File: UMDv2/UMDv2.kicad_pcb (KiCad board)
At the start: 2 copper layers, 128.3 x 83.8 mm, 115 parts, among them CON201 USB-B1HSB6, CON302 JTAG-2X10-HDR, CON303 101-00405-75, CON304 UMDv2-CONN, CON305 HDR1X2, CON306 HDR1X3, SW301 PTS645SM43SMTR92_LFS, U201 MIC5504-3.3YM5-TR, U202 TPS2115APWR, U203 TPS25921ADR, U205 AZ1117CH-3.3TRG1, U207 INA199A2DCKR, U301 STM32F413ZHT6, U302 74ALVC164245DL,118, U303 74ALVC164245DL,118, X301 ECS-80-18-30-JGN-TR

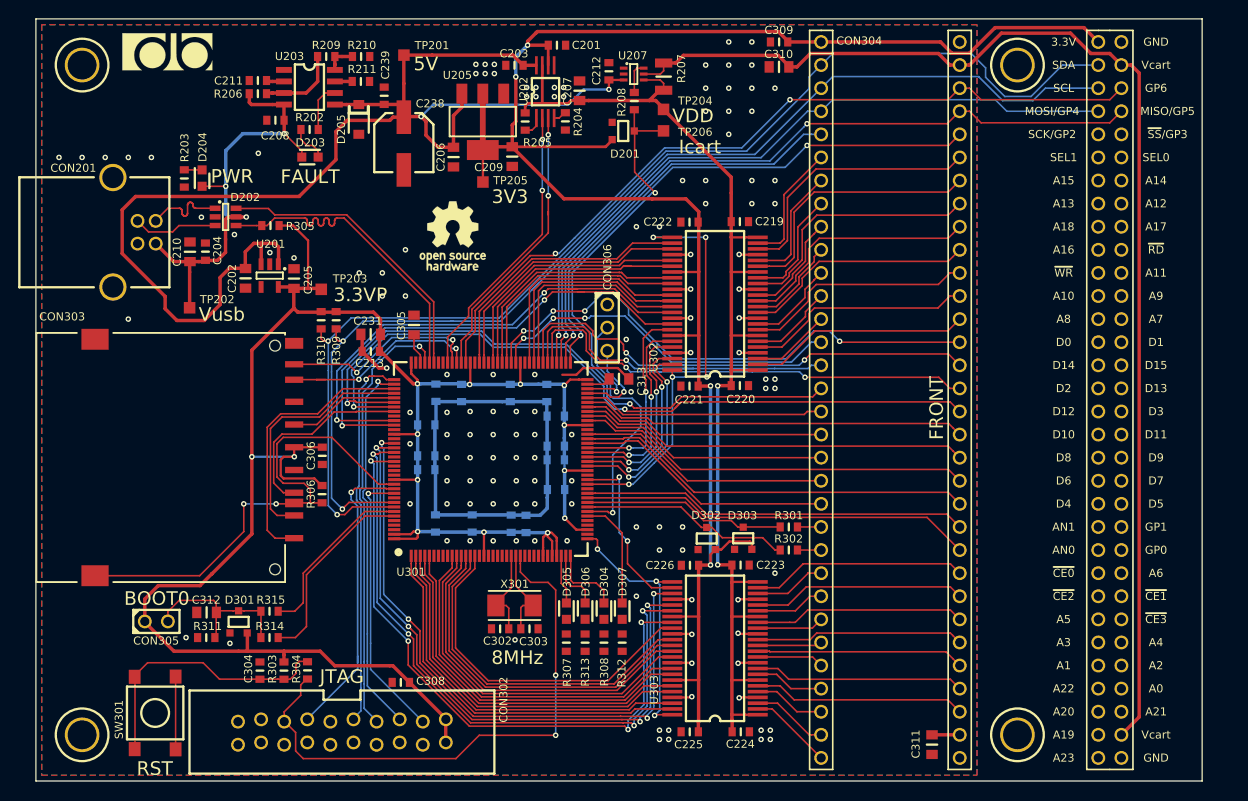
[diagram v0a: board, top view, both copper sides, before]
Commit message: finished LA connector, started review
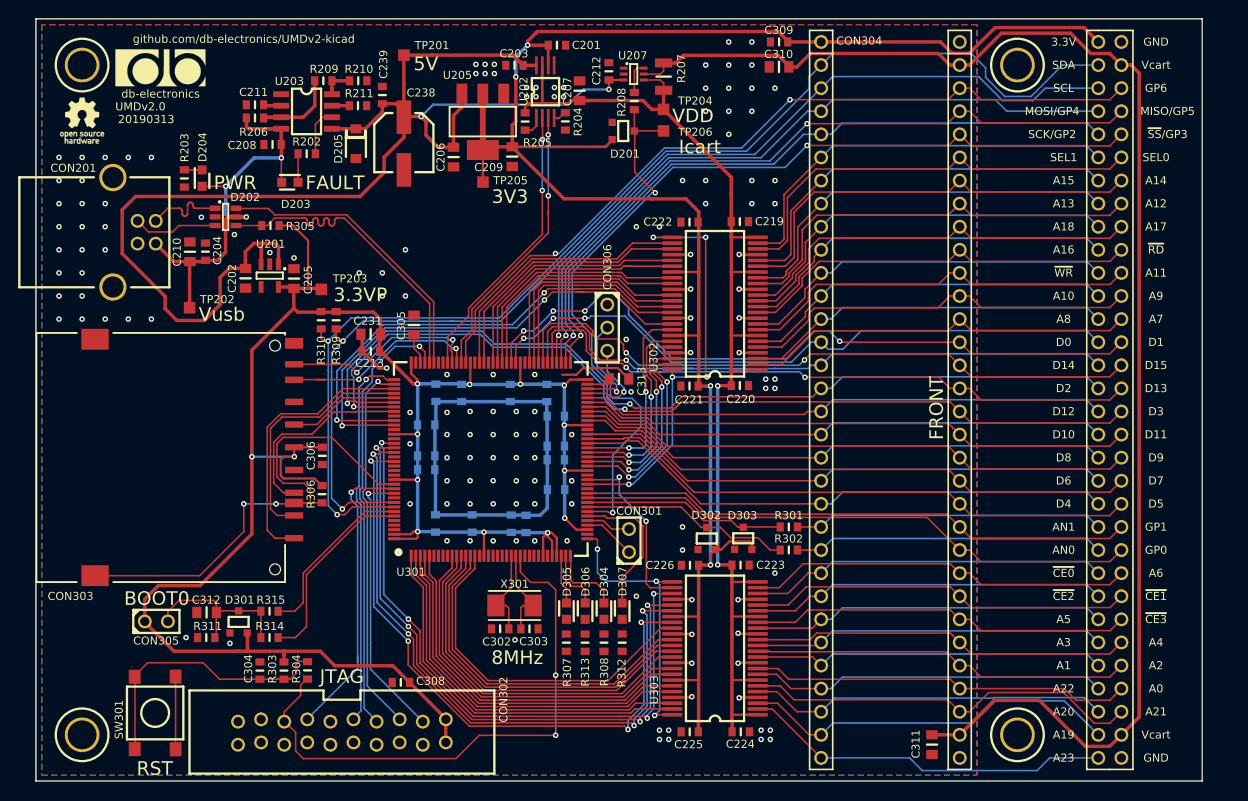
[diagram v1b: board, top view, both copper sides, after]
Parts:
- added CON301: HDR1X2, db-thparts:HDR1X2, F.Cu at (159.1, 120.5)
- logo102: footprint db-artwork:oshw-logo_7.5mm -> db-artwork:oshw-logo_5mm
- moved logo102 42.7 mm to (99.0, 73.0)
- moved D203 3.54 mm to (122.7, 79.8)
- moved C211 2.69 mm to (118.0, 71.3)
- moved R202 2.69 mm to (123.7, 76.7)
- moved R206 2.69 mm to (118.0, 72.7)
- moved C208 2.69 mm to (119.9, 75.6)
- moved D205 2.69 mm to (129.1, 73.9)
- moved R211 2.69 mm to (129.3, 71.4)
- moved U203 2.69 mm to (120.9, 70.1)
- moved R209 2.69 mm to (125.5, 68.6)
- moved R210 2.69 mm to (129.4, 68.6)
- moved logo101 1.92 mm to (107.6, 67.2)
- moved C239 0.22 mm to (132.0, 70.2)
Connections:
- D304 pad 2: /Microcontroller/LED2 -> /Microcontroller/LED1
- D305 pad 2: /Microcontroller/LED0 -> /Microcontroller/LED3
- D306 pad 2: /Microcontroller/LED1 -> /Microcontroller/LED2
- D307 pad 2: /Microcontroller/LED3 -> /Microcontroller/LED0
- U301 pad 34: /Microcontroller/LED0 -> /Microcontroller/LED3
- U301 pad 35: /Microcontroller/LED1 -> /Microcontroller/LED2
- U301 pad 36: /Microcontroller/LED2 -> /Microcontroller/LED1
- U301 pad 42: /Microcontroller/LED3 -> /Microcontroller/LED0
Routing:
- net /Microcontroller/UA19: track 8.41 -> 42.0 mm
- net /Microcontroller/D0: track 39.8 -> 71.9 mm
- net /Microcontroller/UA20: track 7.89 -> 39.7 mm
- net /Microcontroller/UA23: track 9.20 -> 40.8 mm
- net /Microcontroller/USEL1: track 13.7 -> 45.3 mm
- net /Microcontroller/D8: track 27.6 -> 59.2 mm
- net /Microcontroller/D4: track 28.7 -> 60.2 mm
- net /Microcontroller/D12: track 26.6 -> 58.2 mm
- net /Microcontroller/~UCE0~: track 7.91 -> 39.4 mm
- net /Microcontroller/UA5: track 7.37 -> 38.9 mm
- net /Microcontroller/UA13: track 12.7 -> 44.2 mm
- net /Microcontroller/UA3: track 7.11 -> 38.6 mm
- net /Microcontroller/UA1: track 7.36 -> 38.9 mm
- net /Microcontroller/UA16: track 10.3 -> 41.9 mm
- net /Microcontroller/D14: track 40.2 -> 71.8 mm
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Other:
- board text added: "20190313"
- board text added: "UMDv2.0"
- board text added: "db-electronics"
- board text added: "github.com/db-electronics/UMDv2-kicad"

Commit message: working on GND planes
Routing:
- net Vcart: track 159.6 -> 167.2 mm
- net Net-(D305-Pad1): track 0.04 -> 1.66 mm
- net Net-(D306-Pad1): track 0.00 -> 1.62 mm
- net Net-(D307-Pad1): track 0.00 -> 1.62 mm
- net Net-(D304-Pad1): track 0.00 -> 1.62 mm
- net /Microcontroller/UA21: track 44.0 -> 42.9 mm
- net GND: vias 148 -> 168

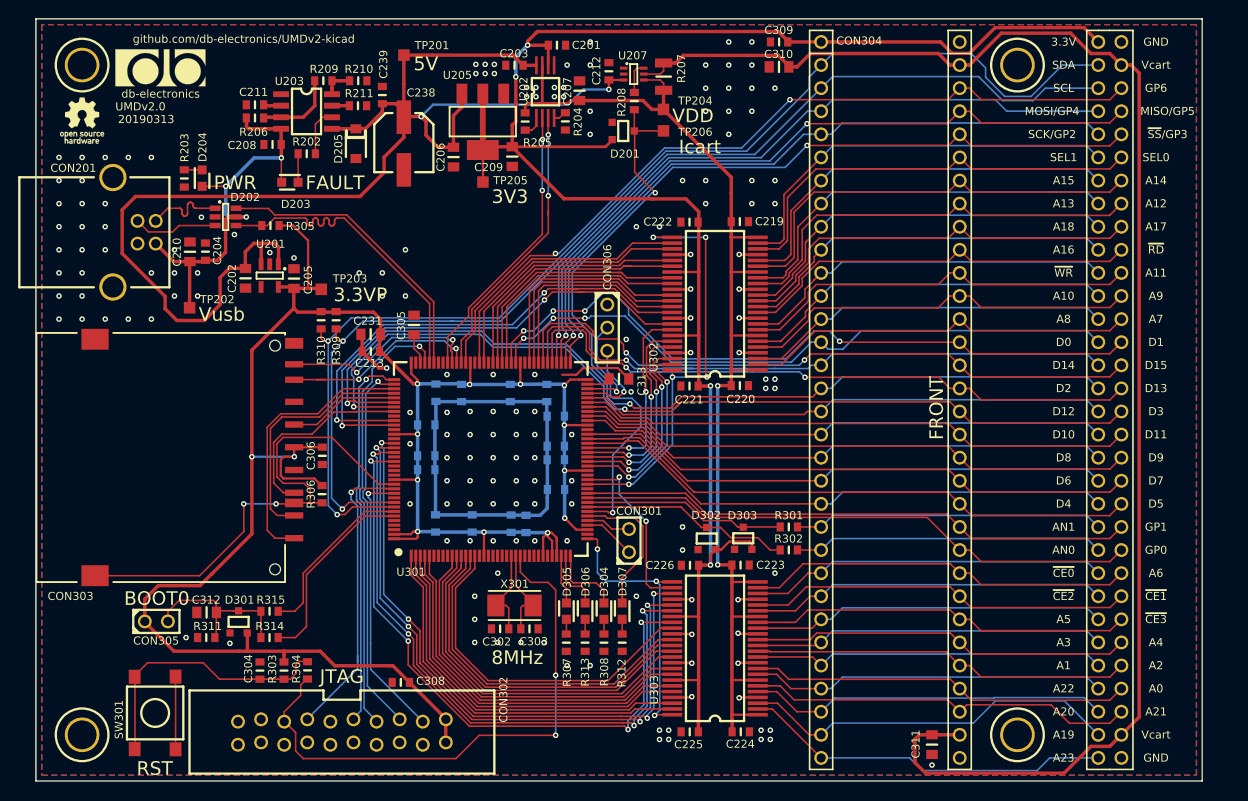
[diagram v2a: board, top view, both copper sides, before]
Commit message: updated UMDv2 symbol and footprint, changed AN0-AN1 to A24, A25
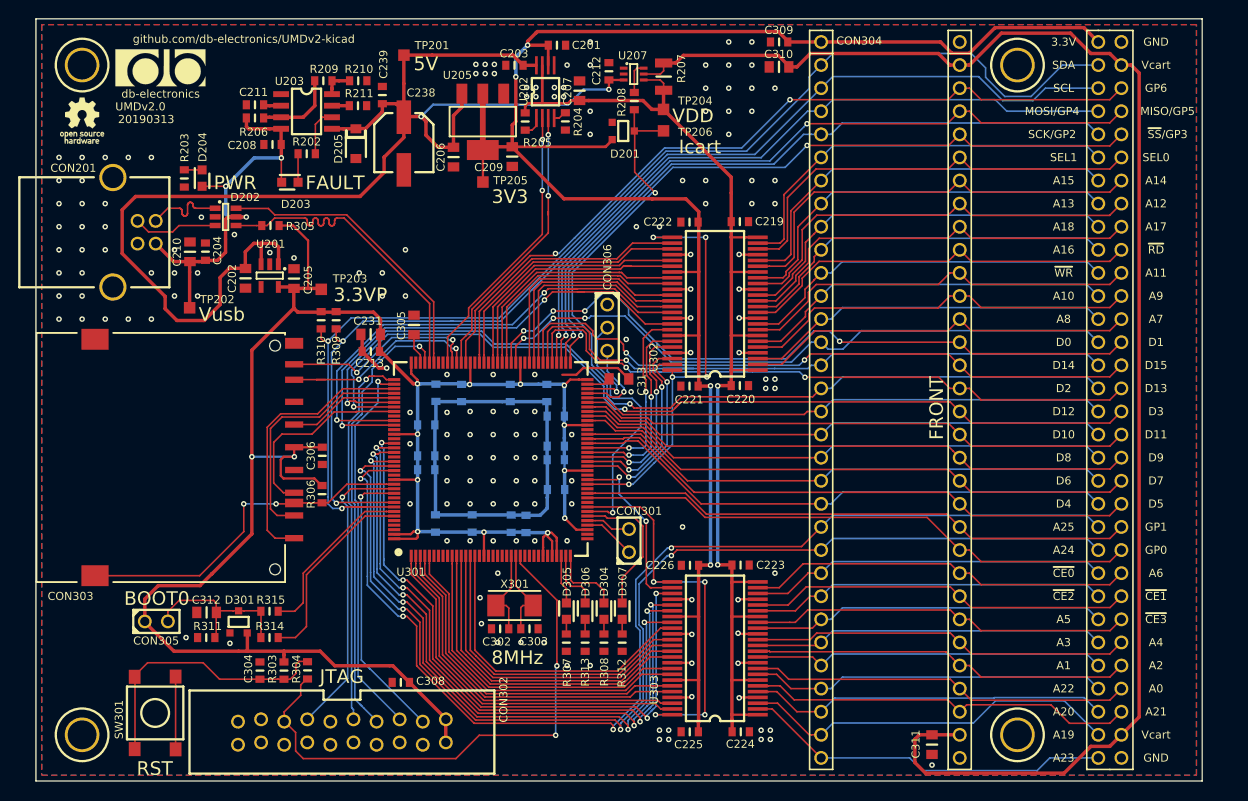
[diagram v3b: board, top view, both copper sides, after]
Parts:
- removed D302, D303: BAT54S, db-smt:SOT23
- removed R301, R302: 100, db-smt:0603
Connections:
- net /Microcontroller/USR_BTN renamed Net-(U301-Pad135)
- CON304 pad 22: Net-(CON304-Pad22) -> /Microcontroller/A25
- CON304 pad 23: Net-(CON304-Pad23) -> /Microcontroller/A24
- U301 pad 128: Net-(U301-Pad128) -> /Microcontroller/A24
- U301 pad 129: Net-(U301-Pad129) -> /Microcontroller/A25
- U301 pad 37: /Microcontroller/~OUT_EN0~ -> Net-(U301-Pad37)
- U301 pad 44: /Microcontroller/AN0 -> /Microcontroller/~OUT_EN0~
- U301 pad 45: /Microcontroller/AN1 -> Net-(U301-Pad45)
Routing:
- net /Microcontroller/A25: track 0.00 -> 125.0 mm, vias 0 -> 4
- net /Microcontroller/A24: track 0.00 -> 124.3 mm, vias 0 -> 4
- net Net-(CON304-Pad23): track 34.1 -> 0.00 mm
- net Net-(CON304-Pad22): track 34.1 -> 0.00 mm
- net /Microcontroller/AN0: track 23.2 -> 0.00 mm
- net /Microcontroller/AN1: track 22.3 -> 0.00 mm
- net /Microcontroller/~SDCD~: track 54.9 -> 39.2 mm
- net /Microcontroller/~OUT_EN0~: track 30.5 -> 44.3 mm, vias 3 -> 4
- net +3V3: track 209.8 -> 202.8 mm
- net /Microcontroller/A5: track 38.7 -> 35.0 mm
- net /Microcontroller/A4: track 38.9 -> 35.3 mm
- net /Microcontroller/A3: track 39.3 -> 35.8 mm
- net /Microcontroller/A2: track 39.7 -> 36.3 mm
- net /Microcontroller/A1: track 40.1 -> 36.9 mm
- net /Microcontroller/A0: track 40.3 -> 37.1 mm
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
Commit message: optimizing signals, re-arranged A24/A25 and several GPx on UMDv2 connector
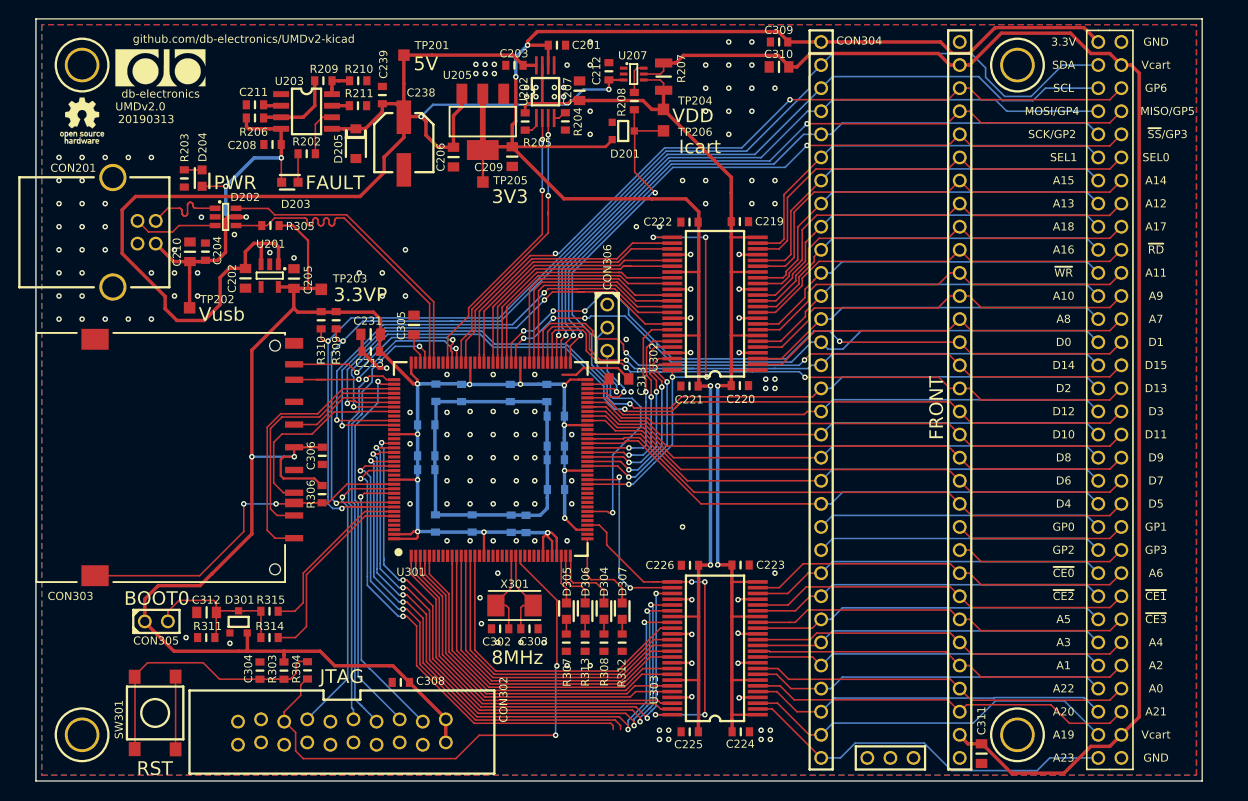
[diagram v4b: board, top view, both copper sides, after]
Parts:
- removed CON301: HDR1X2, db-thparts:HDR1X2
- moved C311 5.54 mm to (197.9, 141.6)
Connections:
- net /Microcontroller/GP6 renamed /Microcontroller/GP8
- CON304 pad 22: /Microcontroller/A25 -> /Microcontroller/GP0
- CON304 pad 23: /Microcontroller/A24 -> /Microcontroller/GP2
- CON304 pad 42: /Microcontroller/GP0 -> /Microcontroller/GP3
- R309 pad 1: +3.3VP -> Net-(R309-Pad1)
- R309 pad 2: /Microcontroller/SCL1 -> Net-(R309-Pad2)
- R310 pad 1: +3.3VP -> Net-(R310-Pad1)
- U301 pad 37: Net-(U301-Pad37) -> /Microcontroller/LED0
- U301 pad 40: /Microcontroller/DAC1 -> /Microcontroller/~OUT_EN0~
- U301 pad 41: /Microcontroller/DAC2 -> Net-(U301-Pad41)
- U301 pad 42: /Microcontroller/LED0 -> Net-(U301-Pad42)
- U301 pad 44: /Microcontroller/~OUT_EN0~ -> /Microcontroller/GP2
- U301 pad 45: Net-(U301-Pad45) -> /Microcontroller/GP3
- U301 pad 7: Net-(U301-Pad7) -> /Microcontroller/~DTCT~
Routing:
- net /Microcontroller/A25: track 125.0 -> 52.8 mm, vias 4 -> 2
- net /Microcontroller/A24: track 124.3 -> 54.0 mm, vias 4 -> 2
- net /Microcontroller/GP1: track 61.3 -> 18.8 mm
- net /Microcontroller/GP2: track 0.00 -> 31.5 mm
- net /Microcontroller/GP0: track 62.2 -> 31.5 mm
- net /Microcontroller/GP3: track 0.00 -> 18.8 mm
- net Vcart: track 167.2 -> 155.8 mm
- net /Microcontroller/~OUT_EN0~: track 44.3 -> 38.2 mm
- net /Microcontroller/LED0: track 16.0 -> 10.1 mm
- net /Microcontroller/DAC1: track 5.81 -> 0.00 mm
- net /Microcontroller/DAC2: track 4.96 -> 0.00 mm
- net /Microcontroller/A6: track 19.6 -> 21.3 mm
- net /Microcontroller/UA23: track 40.8 -> 42.2 mm
- net GND: vias 165 -> 164

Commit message: genesis cart adapter work
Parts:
- added R301: 2.20k, db-smt:0603, F.Cu at (147.7, 140.7)
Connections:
- CON304 pad 2: /Microcontroller/SDA1 -> /Microcontroller/SCL1
- CON304 pad 3: /Microcontroller/SCL1 -> /Microcontroller/SDA1
- R309 pad 1: Net-(R309-Pad1) -> +3.3VP
- R309 pad 2: Net-(R309-Pad2) -> /Microcontroller/SDA1
- R310 pad 1: Net-(R310-Pad1) -> +3.3VP
- R310 pad 2: /Microcontroller/SDA1 -> /Microcontroller/SCL1
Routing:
- net /Microcontroller/~DTCT~: track 0.00 -> 61.2 mm, vias 0 -> 2
- net /Microcontroller/GP3: track 18.8 -> 62.0 mm
- net /Microcontroller/GP1: track 18.8 -> 61.3 mm
- net /Microcontroller/GP2: track 31.5 -> 59.2 mm
- net /Microcontroller/GP0: track 31.5 -> 58.6 mm
- net /Microcontroller/A25: track 52.8 -> 72.8 mm
- net /Microcontroller/A24: track 54.0 -> 73.9 mm
- net +3.3VP: track 242.1 -> 250.1 mm
- net /Microcontroller/SCL1: track 124.9 -> 129.9 mm
- net /Microcontroller/UA23: track 42.2 -> 45.5 mm
- net /Microcontroller/SDA1: track 131.4 -> 128.7 mm, vias 2 -> 3
- net /Microcontroller/~RST: track 61.0 -> 62.9 mm
- net /Microcontroller/UA19: track 42.0 -> 43.8 mm
- net GND: vias 164 -> 159

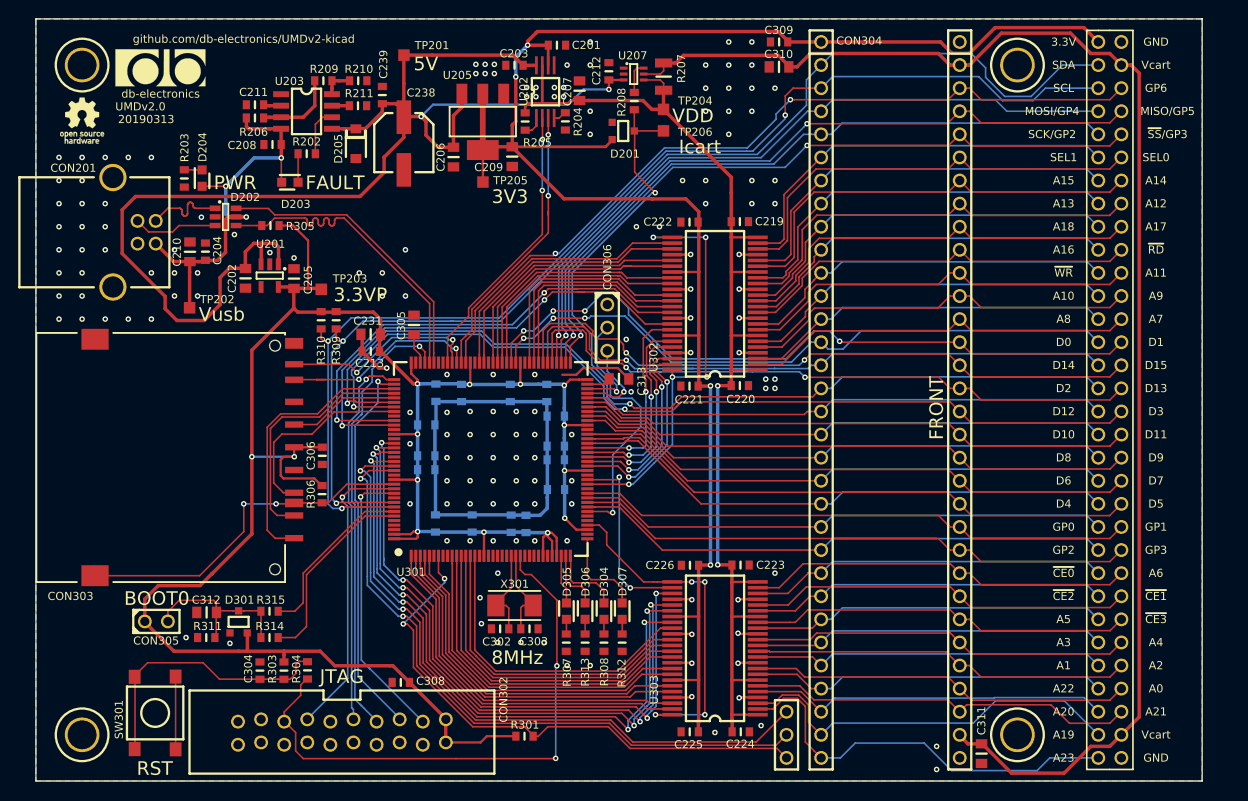
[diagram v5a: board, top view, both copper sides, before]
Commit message: increased spacing on UMDv2 connector
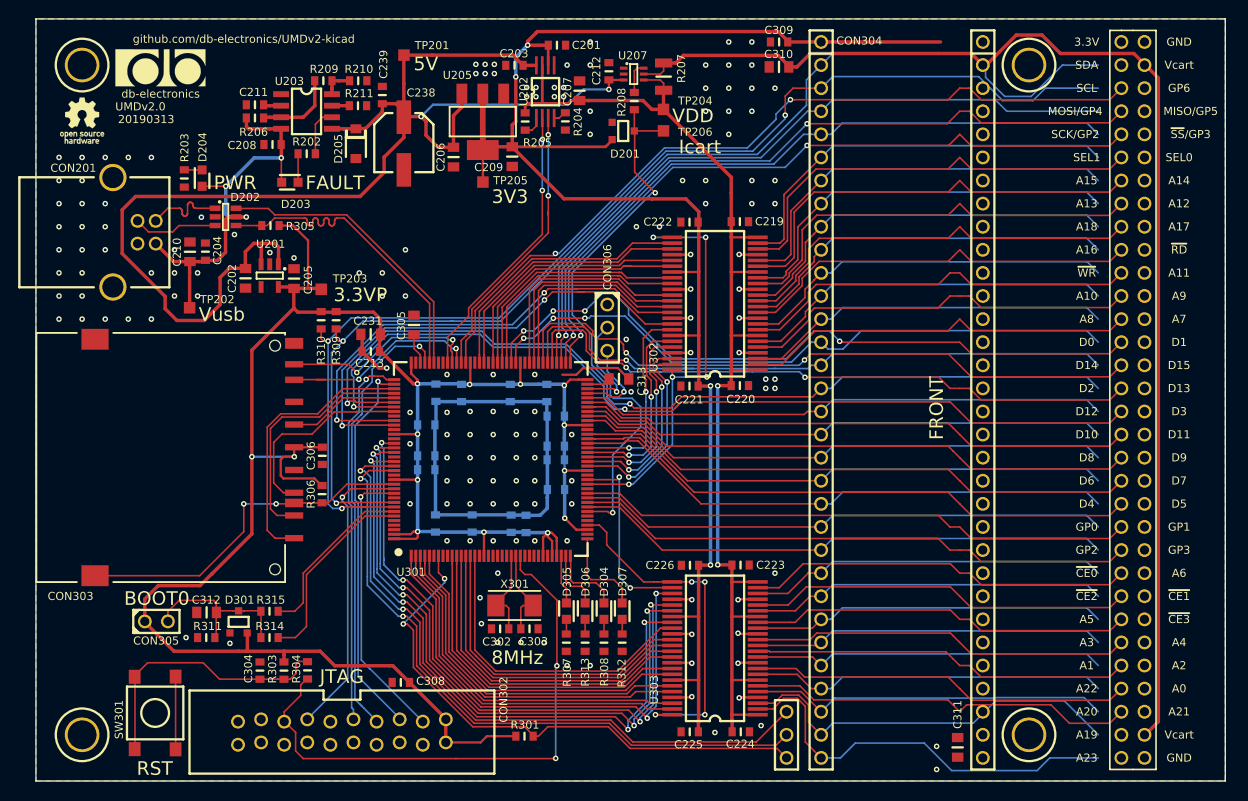
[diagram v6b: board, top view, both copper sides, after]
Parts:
- moved C311 2.72 mm to (195.3, 140.9)
- moved MEC102 1.27 mm to (203.1, 66.9)
- moved MEC104 1.27 mm to (203.1, 140.6)
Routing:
- net Vcart: track 155.8 -> 136.0 mm
- net +3V3: track 202.8 -> 183.1 mm
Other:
- board size 128.3 x 83.8 mm -> 130.8 x 83.8 mm
